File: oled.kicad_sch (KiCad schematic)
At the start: 23 parts, among them Q3 IRLML6402, Q4 BSS138, Q5 BSS138, U7 AP3012KTR-E1

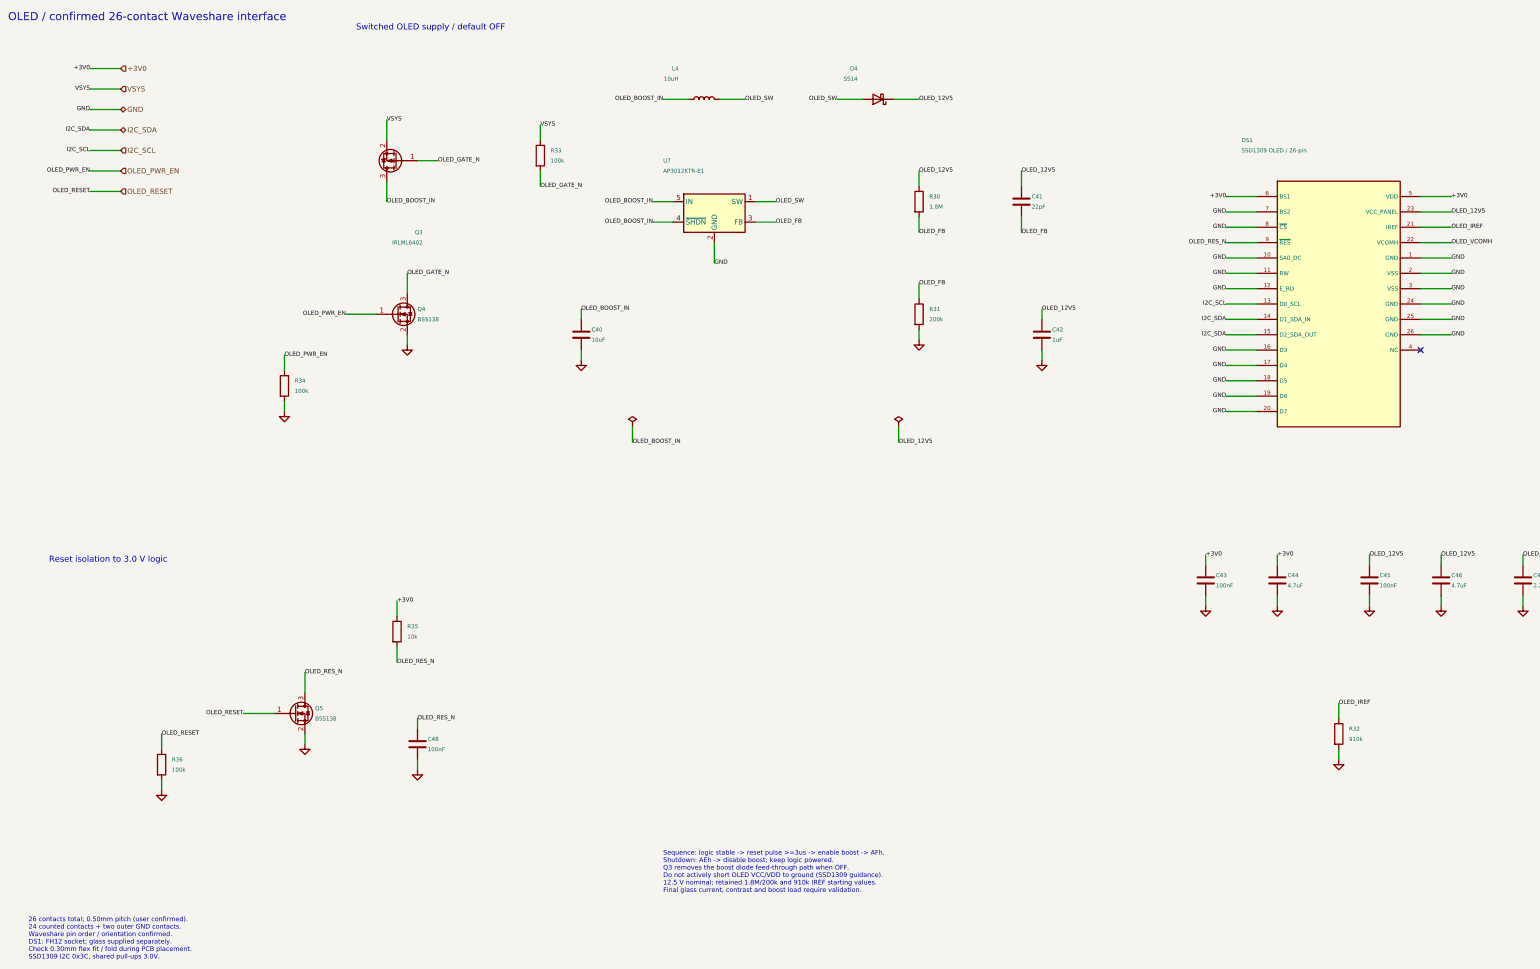
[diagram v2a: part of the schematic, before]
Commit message: Correct OLED interface and routing for 24-pin display
Replace the 26-contact OLED symbol and socket with the verified CON24 pinout and Hirose FH12-24S connector. Preserve DS1 placement and all other board geometry while rerouting its local pad escapes. Update purchasing data, design exports and regression checks.

Validation: zero ERC/DRC errors, no unconnected items or schematic parity issues; 54 layout/regression checks pass; all 261 scoped simulation results unchanged. The two existing U3 silkscreen-edge warnings remain.
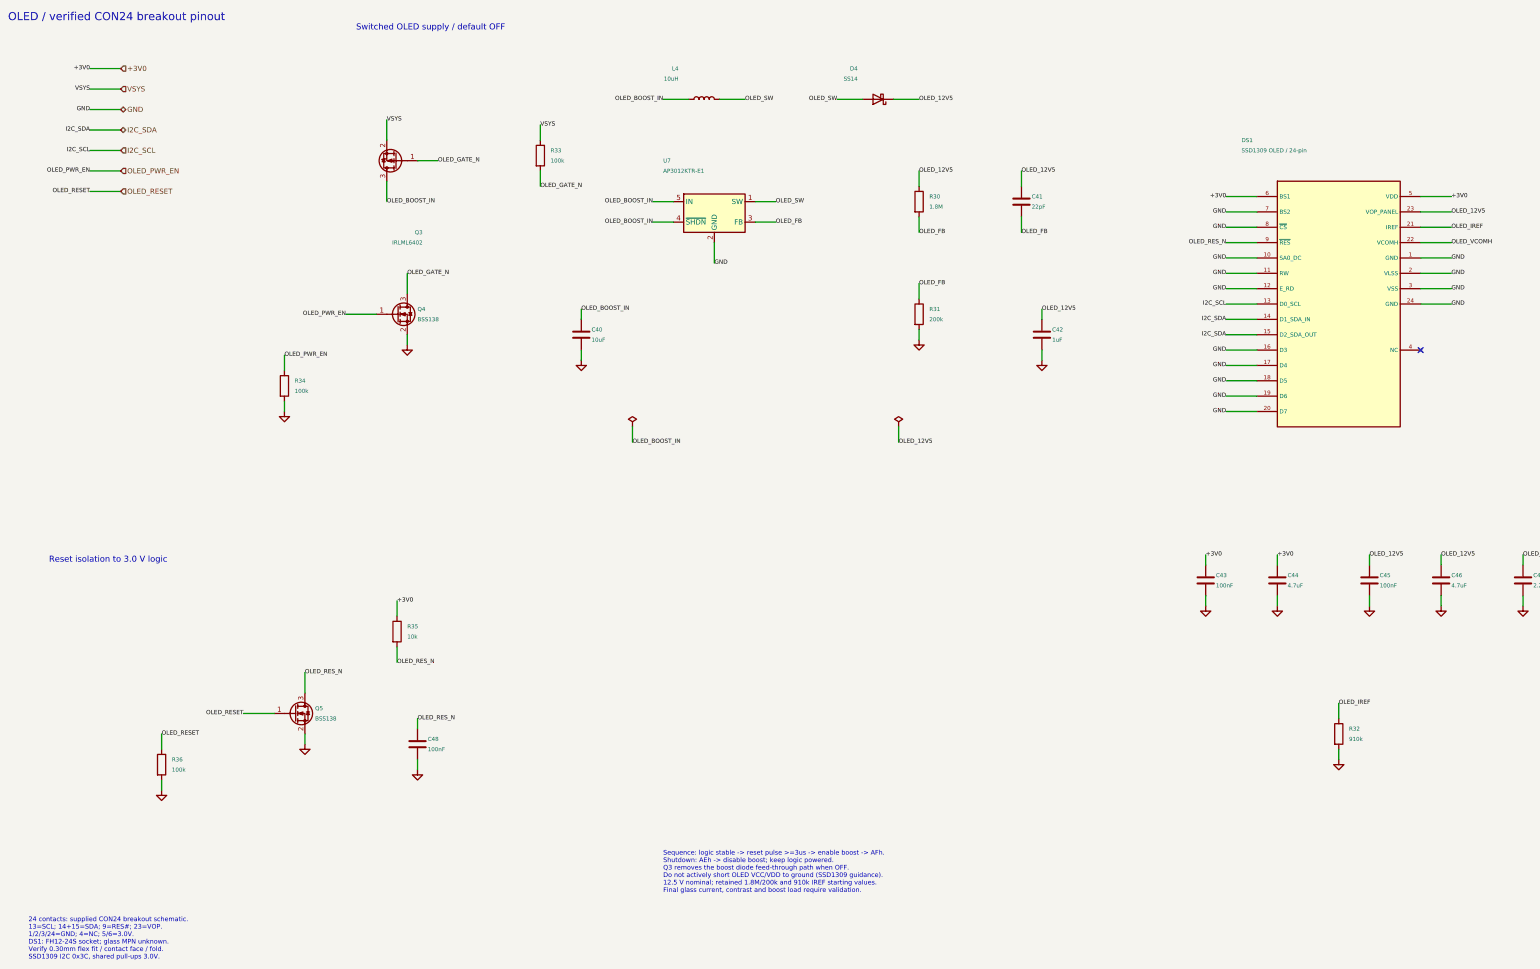
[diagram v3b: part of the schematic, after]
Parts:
- DS1: value SSD1309 OLED / 26-pin -> SSD1309 OLED / 24-pin; footprint Connector_FFC-FPC:Hirose_FH12-26S-0.5SH_1x26-1MP_P0.50mm_Horizontal -> Connector_FFC-FPC:Hirose_FH12-24S-0.5SH_1x24-1MP_P0.50mm_Horizontal; symbol Nucula_Project:SSD1309_COG_26 -> Nucula_Project:SSD1309_COG_24; Actual Flex 26 contacts total: 24 counted plus two outer GND contacts; 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 -> 24 contacts per user and supplied CON24 schematic; retained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; Connector Datasheet https://www.hirose.com/product/p/CL0586-0576-2-55 -> https://www.hirose.com/product/p/CL0586-0521-0-55; Connector Mechanics FH12 bottom-contact, 0.30 mm flex thickness; check insertio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 -> FH12 bottom-contact, 0.30 mm flex thickness; verify panel f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; Footprint Status SELECTED: 26-way 0.50 mm; user confirms Waveshare pin order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 -> SELECTED: 24-way 0.50 mm bottom-contact socket; electrical 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; LCSC C202113 -> C202112; MPN FH12-26S-0.5SH(55) -> FH12-24S-0.5SH(55); Status Pinout/orientation confirmed by user; DS1 BOM part is the F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 -> 24-pin electrical map verified against supplied breakout; D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
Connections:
- net GND: no longer DS1.25 (GND), DS1.26 (GND)
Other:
- note added: "24 contacts: supplied CON24 breakout schematic. 13=SCL; 14+15=SDA; 9=RES#; 23=VOP. 1/2/3/24=GND; 4=NC; 5/6=3.0V. DS1: FH12-24S socket; glass MPN unknown. Verify 0.30mm flex fit / contact face / fold. SSD1309 I2C 0x3C, shared pull-ups 3.0V."
- note added: "OLED / verified CON24 breakout pinout"
- note removed: "26 contacts total; 0.50mm pitch (user confirmed). 24 counted contacts + two outer GND contacts. Waveshare pin order / orientation confirmed. DS1: FH12 socket; glass supplied separately. Check 0.30mm flex fit / fold during PCB placement. SSD1309 I2C 0x3C, shared pull-ups 3.0V."
- note removed: "OLED / confirmed 26-contact Waveshare interface"
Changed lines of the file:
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@@
     (rev "B-draft")
   )
-  (text "OLED / confirmed 26-contact Waveshare interface"
+  (text "OLED / verified CON24 breakout pinout"
     (at 15.24 17.78 0)
     (effects
@@
   )
   (symbol
-    (lib_id "Nucula_Project:SSD1309_COG_26")
+    (lib_id "Nucula_Project:SSD1309_COG_24")
     (at 345.44 88.9 0)
     (unit 1)
@@
       )
     )
-    (property "Value" "SSD1309 OLED / 26-pin"
+    (property "Value" "SSD1309 OLED / 24-pin"
       (at 321.31 50.8 0)
       (effects
@@
       )
     )
-    (property "Footprint" "Connector_FFC-FPC:Hirose_FH12-26S-0.5SH_1x26-1MP_P0.50mm_Horizontal"
+    (property "Footprint" "Connector_FFC-FPC:Hirose_FH12-24S-0.5SH_1x24-1MP_P0.50mm_Horizontal"
       (at 345.44 88.9 0)
       (effects
@@
       )
     )
-    (property "Datasheet" "https://www.lcsc.com/datasheet/lcsc_datasheet_2410010332_HRS-Hirose-FH12-26S-0-5SH-55_C202113.pdf"
+    (property "Datasheet" "https://www.hirose.com/product/p/CL0586-0521-0-55"
       (at 345.44 88.9 0)
       (effects
@@
       )
     )
-    (property "MPN" "FH12-26S-0.5SH(55)"
+    (property "MPN" "FH12-24S-0.5SH(55)"
       (at 345.44 88.9 0)
       (effects
@@
       )
     )
-    (property "Footprint Status" "SELECTED: 26-way 0.50 mm; user confirms Waveshare pin order/orientation, including outer ground contacts"
+    (property "Footprint Status" "SELECTED: 24-way 0.50 mm bottom-contact socket; electrical pinout checked against supplied CON24 breakout schematic"
       (at 345.44 88.9 0)
       (effects
@@
       )
     )
-    (property "Actual Flex" "26 contacts total: 24 counted plus two outer GND contacts; 0.50 mm pitch; copper on emitting side (user confirmed)"
+    (property "Actual Flex" "24 contacts per user and supplied CON24 schematic; retained 0.50 mm pitch/contact-side assumption; exact glass MPN not yet known"
       (at 345.44 88.9 0)
       (effects
@@
       )
     )
-    (property "Status" "Pinout/orientation confirmed by user; DS1 BOM part is the FPC socket, OLED glass supplied separately"
+    (property "Status" "24-pin electrical map verified against supplied breakout; DS1 BOM is socket; glass MPN and mechanical fit remain to verify"
       (at 345.44 88.9 0)
       (effects
@@
       )
     )
-    (property "Connector Mechanics" "FH12 bottom-contact, 0.30 mm flex thickness; check insertion/fold and physical fit during PCB placement"
+    (property "Connector Mechanics" "FH12 bottom-contact, 0.30 mm flex thickness; verify panel flex thickness, contact face and fold against actual glass"
       (at 345.44 88.9 0)
       (effects
@@
       )
     )
-    (property "Connector Datasheet" "https://www.hirose.com/product/p/CL0586-0576-2-55"
+    (property "Connector Datasheet" "https://www.hirose.com/product/p/CL0586-0521-0-55"
       (at 345.44 88.9 0)
       (effects
@@
     (pin "24"
     )
-    (pin "25"
-    )
-    (pin "26"
-    )
     (pin "4"
     )
@@
       )
     )
-    (property "LCSC" "C202113"
+    (property "LCSC" "C202112"
       (at 345.44 88.9 0)
       (effects
@@
     )
   )
-  (wire
-    (pts
-      (xy 365.76 92.71)
-      (xy 373.38 92.71)
-    )
-    (stroke
-      (width 0)
-      (type default)
-    )
-  )
-  (label "GND"
-    (at 373.38 92.71 0)
-    (effects
-      (font
-        (size 1.05 1.05)
-      )
-      (justify left)
-    )
-  )
-  (wire
-    (pts
-      (xy 365.76 96.52)
-      (xy 373.38 96.52)
-    )
-    (stroke
-      (width 0)
-      (type default)
-    )
-  )
-  (label "GND"
-    (at 373.38 96.52 0)
-    (effects
-      (font
-        (size 1.05 1.05)
-      )
-      (justify left)
-    )
-  )
   (no_connect
     (at 365.76 100.33)
@@
     )
   )
-  (text "26 contacts total; 0.50mm pitch (user confirmed).\n24 counted contacts + two outer GND contacts.\nWaveshare pin order / orientation confirmed.\nDS1: FH12 socket; glass supplied separately.\nCheck 0.30mm flex fit / fold during PCB placement.\nSSD1309 I2C 0x3C, shared pull-ups 3.0V."
+  (text "24 contacts: supplied CON24 breakout schematic.\n13=SCL; 14+15=SDA; 9=RES#; 23=VOP.\n1/2/3/24=GND; 4=NC; 5/6=3.0V.\nDS1: FH12-24S socket; glass MPN unknown.\nVerify 0.30mm flex fit / contact face / fold.\nSSD1309 I2C 0x3C, shared pull-ups 3.0V."
     (at 20.32 246.38 0)
     (effects

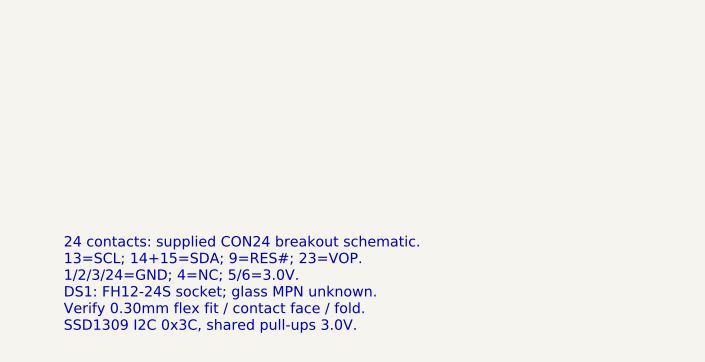
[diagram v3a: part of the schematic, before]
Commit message: Use top-contact OLED connector and document manufacturing preparation
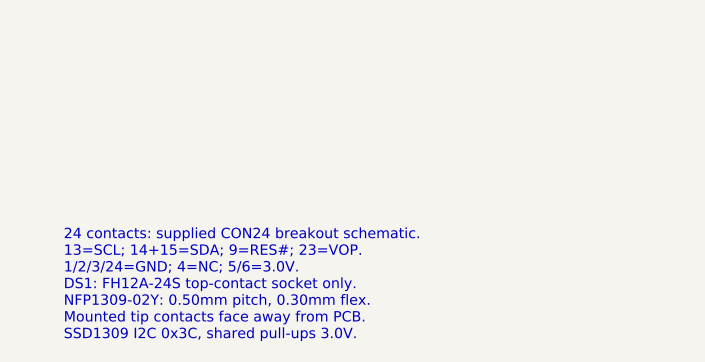
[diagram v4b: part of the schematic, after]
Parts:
- DS1: footprint Connector_FFC-FPC:Hirose_FH12-24S-0.5SH_1x24-1MP_P0.50mm_Horizontal -> Nucula_Project:Hirose_FH12A-24S-0.5SH_1x24-1MP_P0.50mm_Horizontal; Actual Flex 24 contacts per user and supplied CON24 schematic; retained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 -> 24 contacts per user and supplied CON24 schematic; NFP1309-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; Connector Datasheet https://www.hirose.com/product/p/CL0586-0521-0-55 -> https://www.hirose.com/en/product/p/CL0586-0555-2-55; Connector Mechanics FH12 bottom-contact, 0.30 mm flex thickness; verify panel f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 -> FH12A top-contact, 0.30 mm flex, 0.50 mm pitch; same copper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; Footprint Status SELECTED: 24-way 0.50 mm bottom-contact socket; electrical 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 -> SELECTED: 24-way 0.50 mm top-contact socket; Hirose drawing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; LCSC C202112 -> C506794; MPN FH12-24S-0.5SH(55) -> FH12A-24S-0.5SH(55); Status 24-pin electrical map verified against supplied breakout; D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 -> Top-contact socket selected for user-confirmed ribbon orien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
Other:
- note added: "24 contacts: supplied CON24 breakout schematic. 13=SCL; 14+15=SDA; 9=RES#; 23=VOP. 1/2/3/24=GND; 4=NC; 5/6=3.0V. DS1: FH12A-24S top-contact socket only. NFP1309-02Y: 0.50mm pitch, 0.30mm flex. Mounted tip contacts face away from PCB. SSD1309 I2C 0x3C, shared pull-ups 3.0V."
- note removed: "24 contacts: supplied CON24 breakout schematic. 13=SCL; 14+15=SDA; 9=RES#; 23=VOP. 1/2/3/24=GND; 4=NC; 5/6=3.0V. DS1: FH12-24S socket; glass MPN unknown. Verify 0.30mm flex fit / contact face / fold. SSD1309 I2C 0x3C, shared pull-ups 3.0V."
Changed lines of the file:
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@@
       )
     )
-    (property "Footprint" "Connector_FFC-FPC:Hirose_FH12-24S-0.5SH_1x24-1MP_P0.50mm_Horizontal"
+    (property "Footprint" "Nucula_Project:Hirose_FH12A-24S-0.5SH_1x24-1MP_P0.50mm_Horizontal"
       (at 345.44 88.9 0)
       (effects
@@
       )
     )
-    (property "Datasheet" "https://www.hirose.com/product/p/CL0586-0521-0-55"
+    (property "Datasheet" "https://www.hirose.com/en/product/p/CL0586-0555-2-55"
       (at 345.44 88.9 0)
       (effects
@@
       )
     )
-    (property "MPN" "FH12-24S-0.5SH(55)"
+    (property "MPN" "FH12A-24S-0.5SH(55)"
       (at 345.44 88.9 0)
       (effects
@@
       )
     )
-    (property "Footprint Status" "SELECTED: 24-way 0.50 mm bottom-contact socket; electrical pinout checked against supplied CON24 breakout schematic"
+    (property "Footprint Status" "SELECTED: 24-way 0.50 mm top-contact socket; Hirose drawing EDC3-150555-51 sheet 1 lands verified; supplied CON24 electrical map retained"
       (at 345.44 88.9 0)
       (effects
@@
       )
     )
-    (property "Actual Flex" "24 contacts per user and supplied CON24 schematic; retained 0.50 mm pitch/contact-side assumption; exact glass MPN not yet known"
+    (property "Actual Flex" "24 contacts per user and supplied CON24 schematic; NFP1309-02Y ribbon marking; 0.50 mm pitch, 0.30 mm thick; mounted tip contacts face away from PCB"
       (at 345.44 88.9 0)
       (effects
@@
       )
     )
-    (property "Status" "24-pin electrical map verified against supplied breakout; DS1 BOM is socket; glass MPN and mechanical fit remain to verify"
+    (property "Status" "Top-contact socket selected for user-confirmed ribbon orientation; DS1 BOM is socket only; display and keyboard modules excluded; final physical fit and panel operation need prototype verification"
       (at 345.44 88.9 0)
       (effects
@@
       )
     )
-    (property "Connector Mechanics" "FH12 bottom-contact, 0.30 mm flex thickness; verify panel flex thickness, contact face and fold against actual glass"
+    (property "Connector Mechanics" "FH12A top-contact, 0.30 mm flex, 0.50 mm pitch; same copper lands and pin order; larger body/latch checked in layout; open latch height about 3.6 mm"
       (at 345.44 88.9 0)
       (effects
@@
       )
     )
-    (property "Connector Datasheet" "https://www.hirose.com/product/p/CL0586-0521-0-55"
+    (property "Connector Datasheet" "https://www.hirose.com/en/product/p/CL0586-0555-2-55"
       (at 345.44 88.9 0)
       (effects
@@
       )
     )
-    (property "LCSC" "C202112"
+    (property "LCSC" "C506794"
       (at 345.44 88.9 0)
       (effects
@@
     )
   )
-  (text "24 contacts: supplied CON24 breakout schematic.\n13=SCL; 14+15=SDA; 9=RES#; 23=VOP.\n1/2/3/24=GND; 4=NC; 5/6=3.0V.\nDS1: FH12-24S socket; glass MPN unknown.\nVerify 0.30mm flex fit / contact face / fold.\nSSD1309 I2C 0x3C, shared pull-ups 3.0V."
+  (text "24 contacts: supplied CON24 breakout schematic.\n13=SCL; 14+15=SDA; 9=RES#; 23=VOP.\n1/2/3/24=GND; 4=NC; 5/6=3.0V.\nDS1: FH12A-24S top-contact socket only.\nNFP1309-02Y: 0.50mm pitch, 0.30mm flex.\nMounted tip contacts face away from PCB.\nSSD1309 I2C 0x3C, shared pull-ups 3.0V."
     (at 20.32 246.38 0)
     (effects
